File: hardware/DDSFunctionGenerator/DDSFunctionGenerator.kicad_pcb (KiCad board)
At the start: 2 copper layers, 95 x 70 mm, 144 parts, among them J1 Conn_Coaxial, J2 USB_B_Micro, J3 DG128-5.0-02P-14-00A, J4 DG128-5.0-02P-14-00A, J5 Conn_Coaxial, J6 Conn_Coaxial, J7 Conn_01x04_Male, J8 Conn_01x02_Female, Q1 Q_NPN_BEC, Q2 Q_NPN_BEC, Q3 Q_NPN_BEC, SW1 Rotary_Encoder_Switch, T1 Transformer_1P_1S, U1 TC1107-3.3VOA, U2 L7805, U3 L7805, U4 AD9832, U5 STM32F030K6Tx, U6 FT200XD, U7 AD8325, U8 MCP3425A0T-ECH, X1 XO91, Y1 Crystal

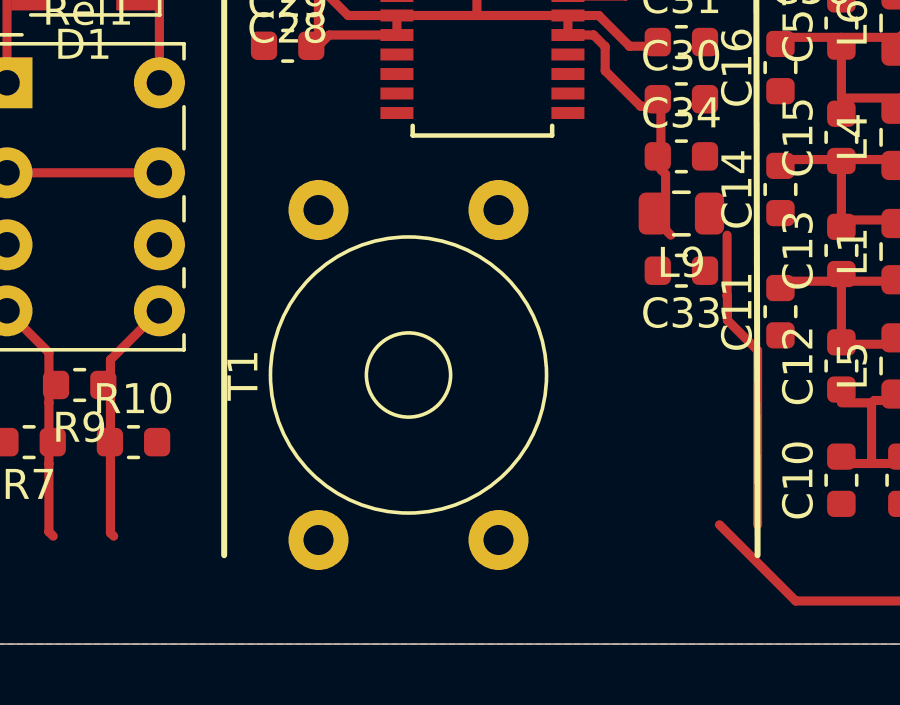
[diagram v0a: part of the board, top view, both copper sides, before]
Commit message: transformer model added
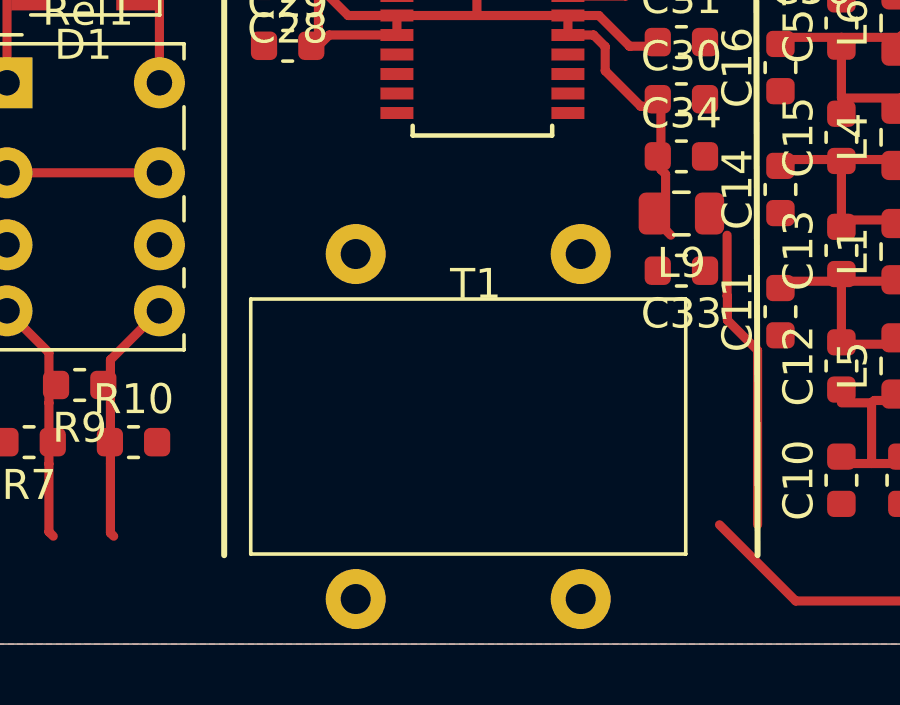
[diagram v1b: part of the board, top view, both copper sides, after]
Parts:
- T1: footprint Transformer_THT:Transformer_Toroid_Horizontal_D9.0mm_Amidon-T30 -> DDSFunctionGenerator:Transformer_B62152_8.3
- moved T1 3.61 mm to (103.0, 128.0), turned to 0 degrees
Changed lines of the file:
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@@
     (add_net TXEN)
   )
+  (module DDSFunctionGenerator:Transformer_B62152_8.3 (layer F.Cu)
+    (at 103 128)
+    (descr Transformer)
+    (tags Transformer)
+    (fp_text reference T1 (at 0 -5 180) (layer F.SilkS)
+      (effects (font (size 1 1) (thickness 0.15)))
+    )
+    (fp_text value Transformer_1P_1S (at 0 5 180) (layer F.Fab)
+      (effects (font (size 1 1) (thickness 0.15)))
+    )
+    (fp_line (start -7.5 4) (end -7.5 -4.5) (layer F.SilkS) (width 0.12))
+    (fp_line (start 7 4) (end -7.5 4) (layer F.SilkS) (width 0.12))
+    (fp_line (start 7 -4.5) (end 7 4) (layer F.SilkS) (width 0.12))
+    (fp_line (start -7.5 -4.5) (end 7 -4.5) (layer F.SilkS) (width 0.12))
+    (fp_text user %R (at 0 -5 180) (layer F.Fab)
+      (effects (font (size 1 1) (thickness 0.15)))
+    )
+    (pad 4 thru_hole circle (at 3.5 5.5) (size 2 2) (drill 1) (layers *.Cu *.Mask)
+      (net 6 GND))
+    (pad 3 thru_hole circle (at -4 5.5) (size 2 2) (drill 1) (layers *.Cu *.Mask)
+      (net 32 RF_FROM_AMPLIFIER))
+    (pad 2 thru_hole circle (at 3.5 -6) (size 2 2) (drill 1) (layers *.Cu *.Mask)
+      (net 33 "Net-(T1-Pad2)"))
+    (pad 1 thru_hole circle (at -4 -6) (size 2 2) (drill 1) (layers *.Cu *.Mask)
+      (net 34 "Net-(T1-Pad1)"))
+    (model ${KISYS3DMOD}/Transformer_THT.3dshapes/Transformer_Toroid_Horizontal_D9.0mm_Amidon-T30.wrl
+      (at (xyz 0 0 0))
+      (scale (xyz 1 1 1))
+      (rotate (xyz 0 0 0))
+    )
+    (model ${KIPRJMOD}/3DModels/Transformer_B62152_8_3.step
+      (at (xyz 0 0 0))
+      (scale (xyz 1 1 1))
+      (rotate (xyz 0 0 0))
+    )
+  )
   (module Capacitor_Tantalum_SMD:CP_EIA-3528-21_Kemet-B (layer F.Cu)
     (at 137.16 93.6125 90)
@@
     )
   )
-  (module Transformer_THT:Transformer_Toroid_Horizontal_D9.0mm_Amidon-T30 (layer F.Cu)
-    (at 103.759 131.532 90)
-    (descr "Transformer, Toroid, horizontal, laying, Diameter 9mm, Amidon, T30,")
-    (tags "Transformer Toroid horizontal laying Diameter 9mm Amidon T30 ")
-    (fp_text reference T1 (at 5.5 -8.5 90) (layer F.SilkS)
-      (effects (font (size 1 1) (thickness 0.15)))
-    )
-    (fp_text value Transformer_1P_1S (at 5.5 3.2 90) (layer F.Fab)
-      (effects (font (size 1 1) (thickness 0.15)))
-    )
-    (fp_circle (center 5.5 -3) (end 10 -3) (layer F.Fab) (width 0.1))
-    (fp_circle (center 5.5 -3) (end 7 -3) (layer F.Fab) (width 0.1))
-    (fp_circle (center 5.5 -3) (end 10.1 -3.1) (layer F.SilkS) (width 0.12))
-    (fp_circle (center 5.5 -3) (end 6.9 -3.1) (layer F.SilkS) (width 0.12))
-    (fp_line (start 12.25 1.75) (end -1.25 1.75) (layer F.CrtYd) (width 0.05))
-    (fp_line (start 12.25 1.75) (end 12.25 -7.75) (layer F.CrtYd) (width 0.05))
-    (fp_line (start -1.25 -7.75) (end -1.25 1.75) (layer F.CrtYd) (width 0.05))
-    (fp_line (start -1.25 -7.75) (end 12.25 -7.75) (layer F.CrtYd) (width 0.05))
-    (fp_line (start 7 -3.5) (end 9.4 -4.8) (layer F.Fab) (width 0.1))
-    (fp_line (start 8.5 -6.1) (end 7 -3.5) (layer F.Fab) (width 0.1))
-    (fp_line (start 6.5 -4.2) (end 8.5 -6.1) (layer F.Fab) (width 0.1))
-    (fp_line (start 7.2 -7) (end 6.5 -4.2) (layer F.Fab) (width 0.1))
-    (fp_line (start 6 -4.5) (end 7.2 -7) (layer F.Fab) (width 0.1))
-    (fp_line (start 5.9 -7.4) (end 6 -4.5) (layer F.Fab) (width 0.1))
-    (fp_line (start 5.3 -4.6) (end 5.9 -7.4) (layer F.Fab) (width 0.1))
-    (fp_line (start 4.5 -7.4) (end 5.3 -4.6) (layer F.Fab) (width 0.1))
-    (fp_line (start 4.7 -4.3) (end 4.5 -7.4) (layer F.Fab) (width 0.1))
-    (fp_line (start 2.8 -6.5) (end 4.7 -4.3) (layer F.Fab) (width 0.1))
-    (fp_line (start 4.1 -3.7) (end 2.8 -6.5) (layer F.Fab) (width 0.1))
-    (fp_line (start 1.5 -5.1) (end 4.1 -3.7) (layer F.Fab) (width 0.1))
-    (fp_line (start 7 -2.5) (end 9.4 -1.1) (layer F.Fab) (width 0.1))
-    (fp_line (start 8.6 0.1) (end 7 -2.5) (layer F.Fab) (width 0.1))
-    (fp_line (start 6.7 -2) (end 8.6 0.1) (layer F.Fab) (width 0.1))
-    (fp_line (start 7.6 0.8) (end 6.7 -2) (layer F.Fab) (width 0.1))
-    (fp_line (start 6.1 -1.6) (end 7.6 0.8) (layer F.Fab) (width 0.1))
-    (fp_line (start 5.9 1.3) (end 6.1 -1.6) (layer F.Fab) (width 0.1))
-    (fp_line (start 5.4 -1.4) (end 5.9 1.3) (layer F.Fab) (width 0.1))
-    (fp_line (start 4.2 1.2) (end 5.4 -1.4) (layer F.Fab) (width 0.1))
-    (fp_line (start 4.7 -1.7) (end 4.2 1.2) (layer F.Fab) (width 0.1))
-    (fp_line (start 2.6 0.2) (end 4.7 -1.7) (layer F.Fab) (width 0.1))
-    (fp_line (start 4.3 -2.2) (end 2.6 0.2) (layer F.Fab) (width 0.1))
-    (fp_line (start 1.6 -0.7) (end 4.3 -2.2) (layer F.Fab) (width 0.1))
-    (fp_text user %R (at 5.5 -8.5 90) (layer F.Fab)
-      (effects (font (size 1 1) (thickness 0.15)))
-    )
-    (pad 4 thru_hole circle (at 11 -6 90) (size 2 2) (drill 1) (layers *.Cu *.Mask)
-      (net 6 GND))
-    (pad 3 thru_hole circle (at 0 -6 90) (size 2 2) (drill 1) (layers *.Cu *.Mask)
-      (net 32 RF_FROM_AMPLIFIER))
-    (pad 2 thru_hole circle (at 11 0 90) (size 2 2) (drill 1) (layers *.Cu *.Mask)
-      (net 33 "Net-(T1-Pad2)"))
-    (pad 1 thru_hole circle (at 0 0 90) (size 2 2) (drill 1) (layers *.Cu *.Mask)
-      (net 34 "Net-(T1-Pad1)"))
-    (model ${KISYS3DMOD}/Transformer_THT.3dshapes/Transformer_Toroid_Horizontal_D9.0mm_Amidon-T30.wrl
-      (at (xyz 0 0 0))
-      (scale (xyz 1 1 1))
-      (rotate (xyz 0 0 0))
-    )
-    (model ${KIPRJMOD}/3DModels/Transformer_Toroid_Horizontal_D9.0mm_Amidon-T30.step
-      (at (xyz 0 0 0))
-      (scale (xyz 1 1 1))
-      (rotate (xyz 0 0 0))
-    )
-  )
   (module Package_TO_SOT_SMD:SOT-23-6_Handsoldering (layer F.Cu)
     (at 125.73 80.708 270)
@@
   (segment (start 130.1405 124.984) (end 129.0857 124.984) (width 0.3048) (layer F.Cu) (net 6))
   (segment (start 129.0857 124.984) (end 127.44335 123.34165) (width 0.3048) (layer F.Cu) (net 6))
+  (segment (start 139.065 124.42) (end 140.589 125.944) (width 0.3048) (layer F.Cu) (net 6))
+  (segment (start 138.557 124.42) (end 139.065 124.42) (width 0.3048) (layer F.Cu) (net 6))
+  (segment (start 140.589 125.412) (end 142.113 123.888) (width 0.3048) (layer F.Cu) (net 6))
+  (segment (start 140.589 125.944) (end 140.589 125.412) (width 0.3048) (layer F.Cu) (net 6))
   (segment (start 122.4945 124.334) (end 121.0565 122.896) (width 0.3048) (layer F.Cu) (net 7))
   (segment (start 124.2405 124.334) (end 122.4945 124.334) (width 0.3048) (layer F.Cu) (net 7))
@@
   (segment (start 136.507 128.031) (end 136.984 128.508) (width 0.3048) (layer F.Cu) (net 43))
   (segment (start 136.507 126.452) (end 136.507 128.031) (width 0.3048) (layer F.Cu) (net 43))
-  (segment (start 139.065 124.42) (end 140.589 125.944) (width 0.3048) (layer F.Cu) (net 6))
-  (segment (start 138.557 124.42) (end 139.065 124.42) (width 0.3048) (layer F.Cu) (net 6))
-  (segment (start 140.589 125.412) (end 142.113 123.888) (width 0.3048) (layer F.Cu) (net 6))
-  (segment (start 140.589 125.944) (end 140.589 125.412) (width 0.3048) (layer F.Cu) (net 6))
   (segment (start 132.801 126.934) (end 132.969 127.102) (width 0.3048) (layer F.Cu) (net 45))
   (segment (start 130.1405 126.934) (end 132.801 126.934) (width 0.3048) (layer F.Cu) (net 45))

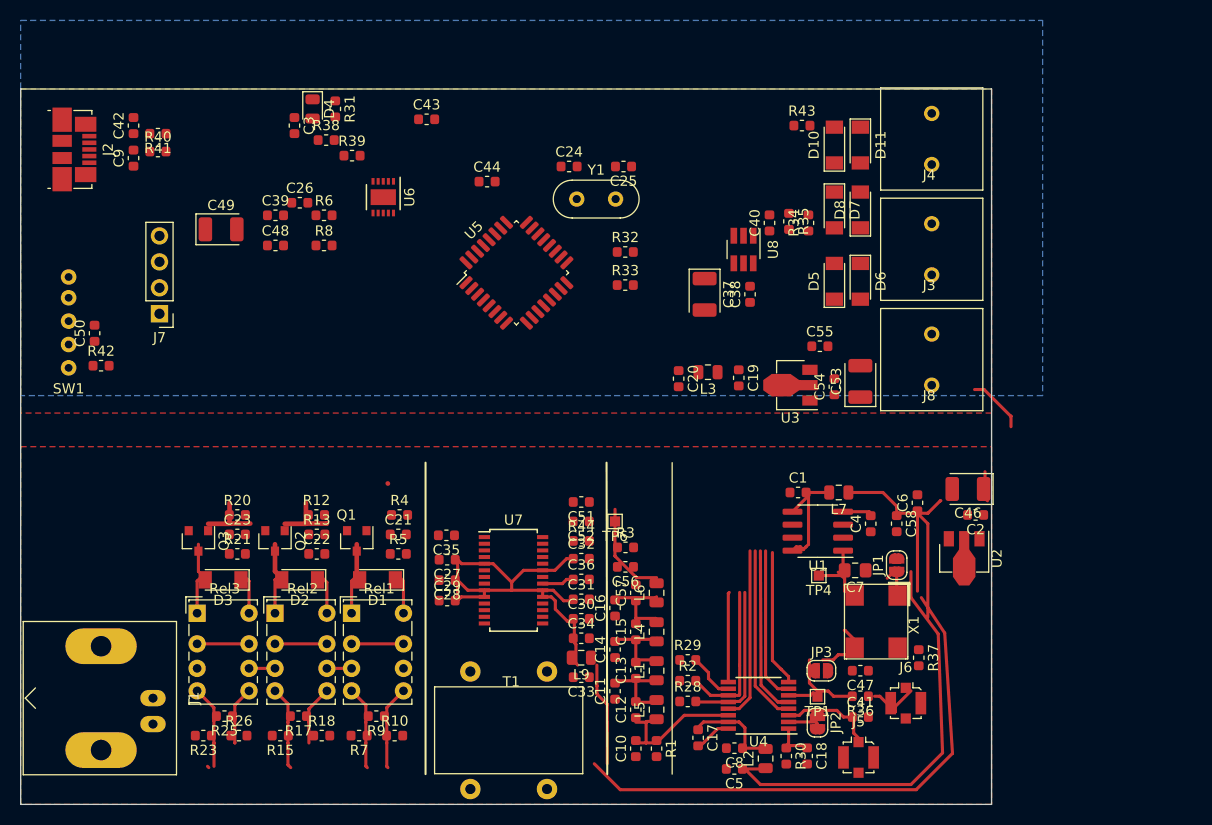
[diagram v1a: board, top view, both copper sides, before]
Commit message: Fully routed RF part.
Signed-off-by: Robert Gawron <robert_gawron@yahoo.fr>
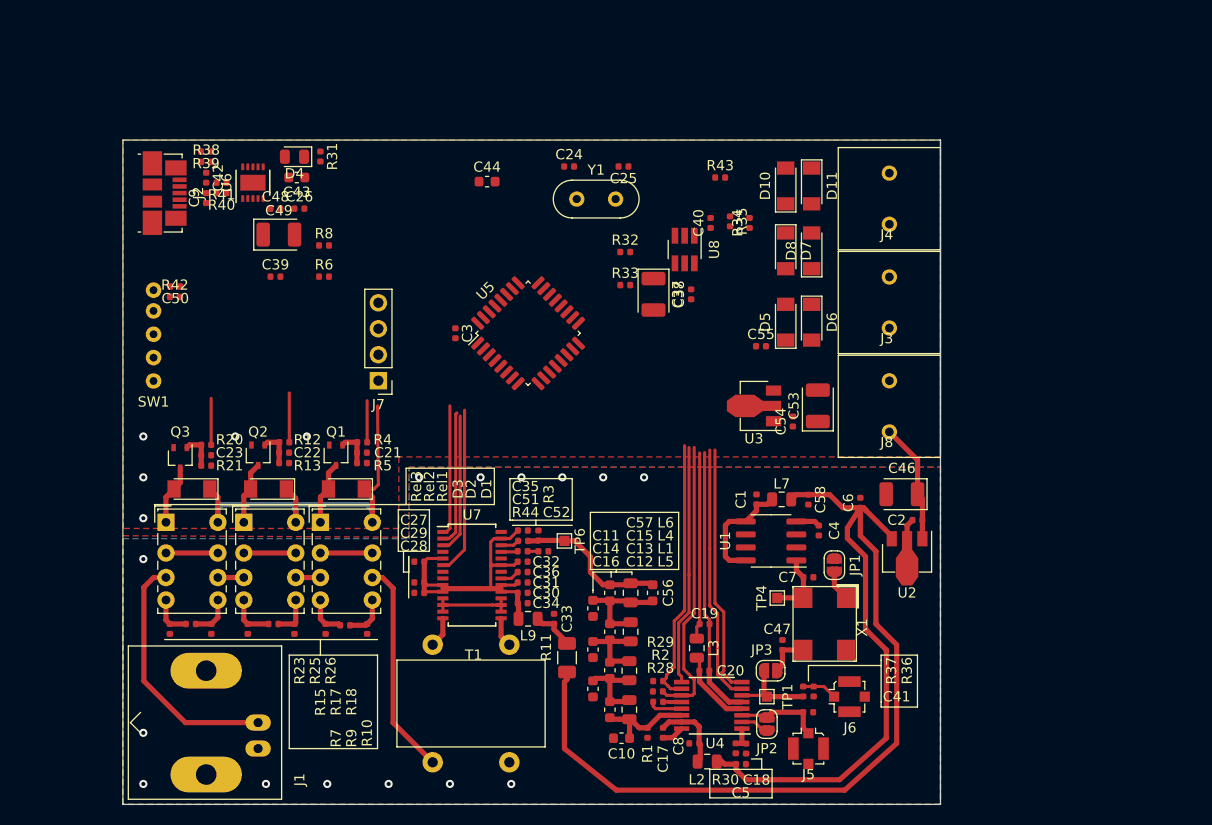
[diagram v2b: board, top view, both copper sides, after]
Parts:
- added R11: 0R, Resistor_SMD:R_1206_3216Metric, F.Cu at (108.5, 120.7)
- C1, C17, C18, C19, C2, C20, C21, C22, C23, C24, C25, C26, C27, C28, C29, C3, C30, C31, C32, C33, C34, C35, C36, C38, C39, C4, C40, C41, C42, C47, C48, C5, C50, C51, C52, C54, C55, C58, C6, C8, C9: footprint Capacitor_SMD:C_0603_1608Metric -> Capacitor_SMD:C_0402_1005Metric
- C7: footprint Capacitor_SMD:C_0805_2012Metric_Pad1.15x1.40mm_HandSolder -> Capacitor_SMD:C_0402_1005Metric
- Q1, Q2, Q3: footprint Package_TO_SOT_SMD:SOT-23 -> Package_TO_SOT_SMD:SOT-323_SC-70
- R1, R10, R12, R13, R15, R17, R18, R2, R20, R21, R23, R25, R26, R28, R29, R3, R30, R31, R32, R33, R34, R35, R36, R37, R38, R39, R4, R40, R41, R42, R43, R44, R5, R6, R7, R8, R9: footprint Resistor_SMD:R_0603_1608Metric -> Resistor_SMD:R_0402_1005Metric
- moved C20 28.7 mm to (121.9, 121.9), turned to 0 degrees
- moved L3 27.0 mm to (121.2, 119.7), turned to 270 degrees
- moved C3 25.7 mm to (97.5, 88.9)
- moved C19 24.3 mm to (121.9, 117.3), turned to 0 degrees
- moved J7 22.4 mm to (90.0, 93.5)
- moved R39 14.3 mm to (73.1, 71.1), turned to 180 degrees
- moved C43 13.9 mm to (82.0, 73.7), turned to 180 degrees
- moved U6 12.8 mm to (77.7, 74.2), turned to 90 degrees
- moved R38 11.9 mm to (73.2, 72.1)
- moved R23 10.9 mm to (69.6, 117.8), turned to 270 degrees
- moved R7 10.9 mm to (84.8, 117.8), turned to 270 degrees
- moved R15 10.9 mm to (77.2, 117.8), turned to 270 degrees
- moved R37 10.8 mm to (132.6, 124.0), turned to 90 degrees
- moved R26 10.8 mm to (73.7, 117.8), turned to 270 degrees
- moved R10 10.8 mm to (88.9, 117.8), turned to 270 degrees
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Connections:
- C33 pad 1: 5V_ANALOG -> Net-(C33-Pad1)
- J8 pad 1: GND -> 9V
- J8 pad 2: 9V -> GND
- L9 pad 1: 5V_ANALOG -> Net-(C33-Pad1)
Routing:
- net 9V: track 20.4 -> 51.7 mm
- net Net-(J1-Pad1): track 0.00 -> 24.6 mm
- net FSELECT: track 4.69 -> 26.0 mm
- net RF_FROM_AMPLIFIER: track 0.00 -> 21.1 mm
- net 5V_DIGITAL: track 0.00 -> 18.3 mm
- net TXEN: track 0.00 -> 16.4 mm
- net FSYNC: track 8.81 -> 23.5 mm
- net SCL: track 0.00 -> 13.7 mm
- net PSEL1: track 14.9 -> 28.2 mm
- net SDA: track 0.00 -> 13.2 mm
- net PSEL0: track 15.2 -> 2.33 mm
- net DATAEN: track 0.00 -> 12.8 mm
- net 5V_ANALOG: track 134.7 -> 123.4 mm
- net SDATA: track 13.3 -> 24.6 mm
- net Net-(C27-Pad1): track 43.3 -> 32.3 mm
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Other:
- board size 95 x 70 mm -> 80 x 65 mm
- net class rf_power_supply added: clearance 0.127, trace_width 0.508, via_dia 0.8, via_drill 0.4

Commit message: encoder footprint draft
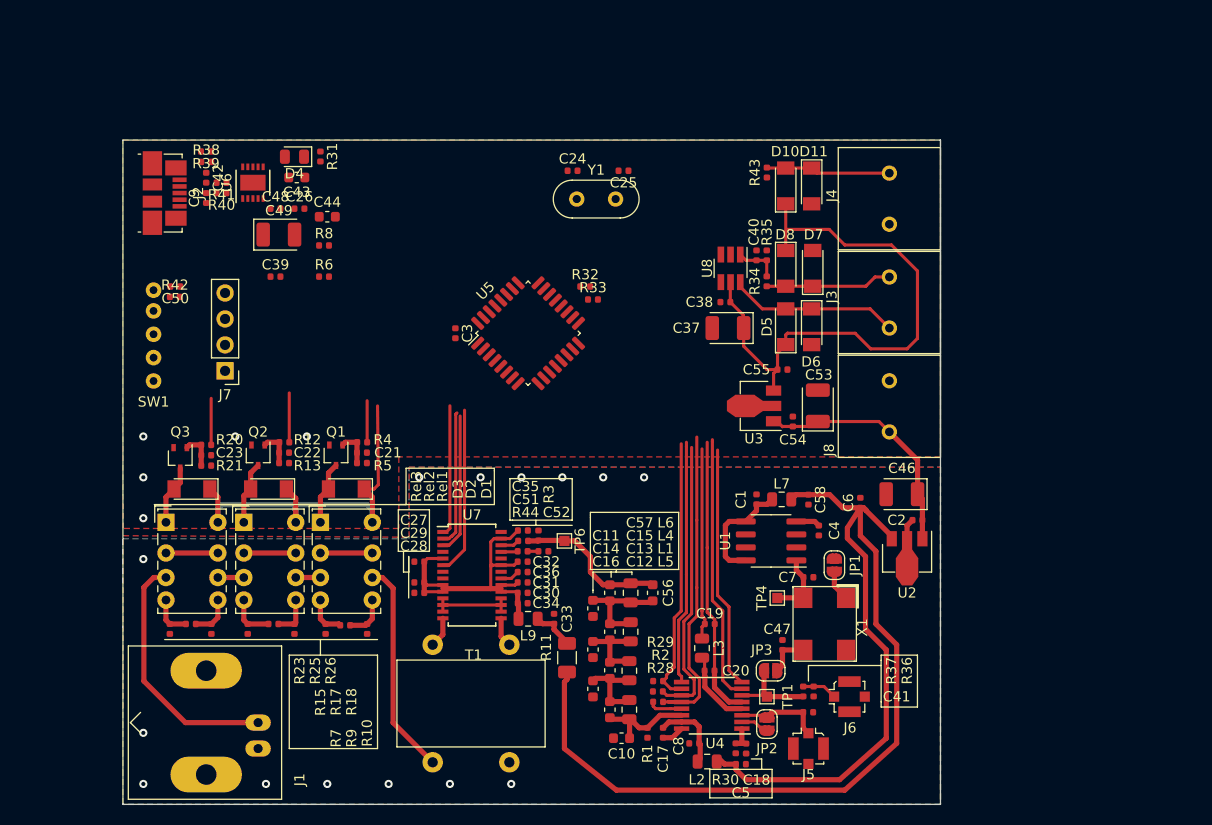
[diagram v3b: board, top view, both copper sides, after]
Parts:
- moved C44 16.0 mm to (85.0, 77.5)
- moved J7 15.0 mm to (75.0, 92.6)
- moved C37 8.00 mm to (124.2, 88.4), turned to 180 degrees
- moved R34 5.96 mm to (128.0, 83.8)
- moved C40 5.50 mm to (127.0, 81.3)
- moved R32 5.18 mm to (110.2, 84.3)
- moved R35 4.89 mm to (128.0, 81.3), turned to 90 degrees
- moved U8 4.86 mm to (124.5, 82.5)
- moved R43 4.60 mm to (128.0, 73.2), turned to 90 degrees
- moved R33 3.46 mm to (111.0, 85.6)
- moved C38 3.43 mm to (124.0, 85.9), turned to 0 degrees
- moved C55 3.11 mm to (129.5, 92.5)
- moved D8 1.72 mm to (132.5, 82.5)
- moved D7 1.72 mm to (129.9, 82.5)
- moved C24 0.54 mm to (109.0, 73.0)
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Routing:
- net 5V_DIGITAL: track 18.3 -> 76.0 mm
- net PSEL0: track 2.33 -> 30.4 mm
- net Net-(D5-Pad2): track 0.00 -> 16.7 mm
- net Net-(D7-Pad2): track 0.00 -> 12.4 mm
- net Net-(D10-Pad2): track 0.00 -> 12.2 mm
- net 9V: track 51.7 -> 63.9 mm
- net Net-(C40-Pad1): track 0.00 -> 4.39 mm
- net GND: track 40.5 -> 41.4 mm
- net SCLK: track 25.3 -> 26.2 mm
- net SDATA: track 24.6 -> 23.7 mm
